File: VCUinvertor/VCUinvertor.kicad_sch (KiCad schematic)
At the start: 96 parts, among them J1 NXP12, J2 NXP11, J3 NXP15, J4 NXP14, J5 NXP10, J6 NXP13, J7 PowerSupply, J8 CAN_NXP, J9 BACKLIGHT, Q1 BSS138, Q10 BSS138, Q2 BSS138, Q3 BSS138, Q4 BSS138, Q5 BSS138, Q6 BSS138, Q7 BSS138, Q8 BSS138, Q9 BSS138, U1 TJA1448ATK, U2 REF3433T, U3 TLV76150DCY

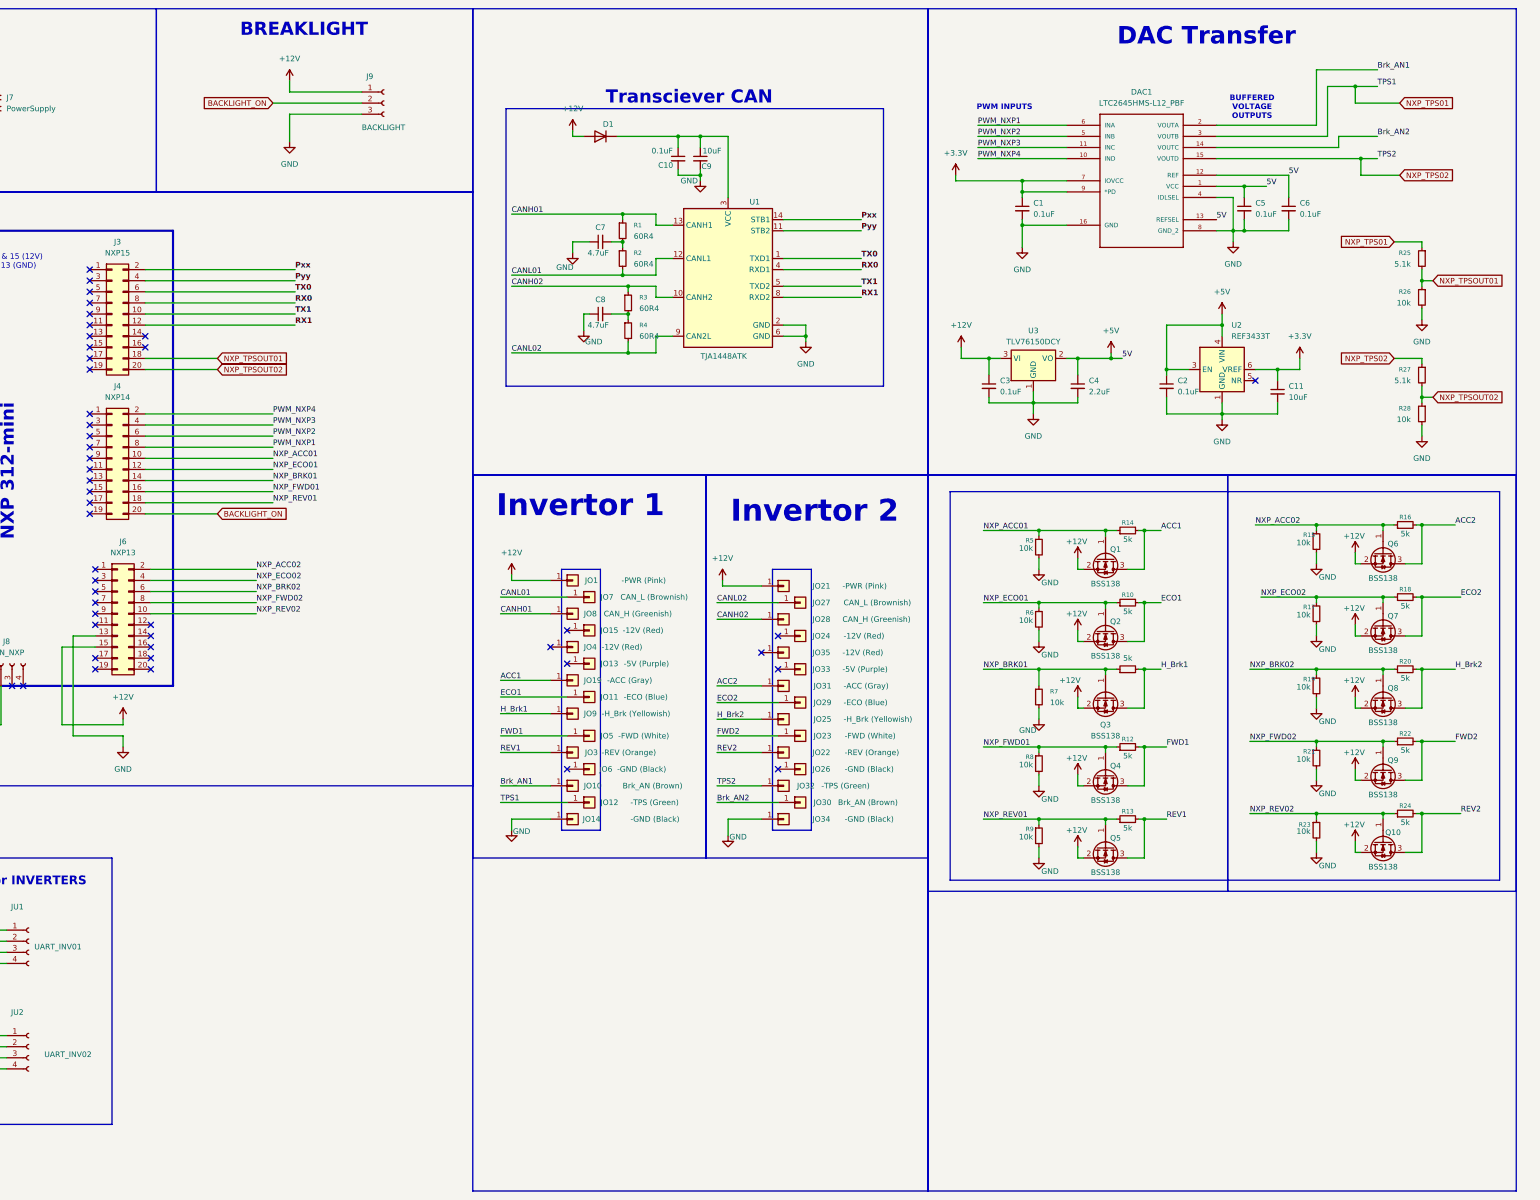
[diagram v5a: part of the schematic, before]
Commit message: New PMOS config for switching
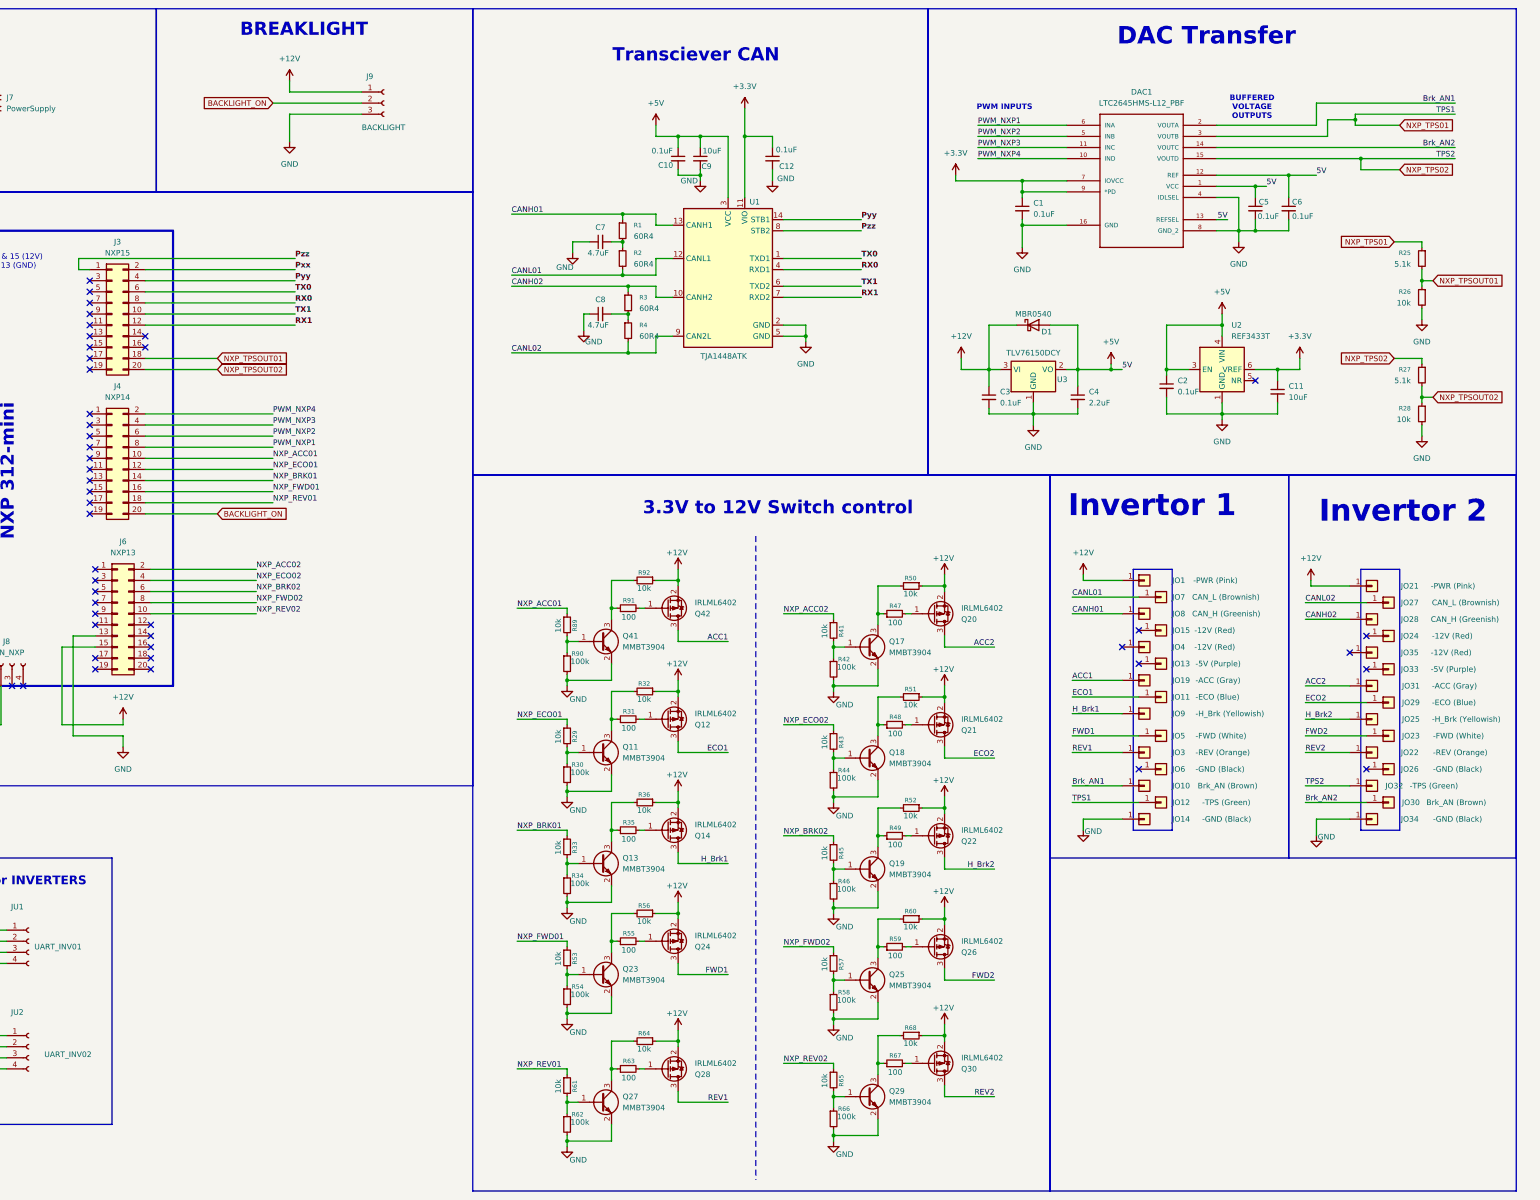
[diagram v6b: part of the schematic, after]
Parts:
- removed D1: 1N4148WT, Diode_SMD:D_SOD-523, symbol Diode:1N4148WT
- removed Q1, Q10, Q2, Q3, Q4, Q5, Q6, Q7, Q8, Q9: BSS138, Package_TO_SOT_SMD:SOT-23, symbol Transistor_FET:BSS138
- removed R10, R11, R12, R13, R14, R16, R18, R20, R22, R24: 5k, Resistor_SMD:R_0805_2012Metric, symbol Device:R_Small
- removed R15, R17, R19, R21, R23, R5, R6, R7, R8, R9: 10k, Resistor_SMD:R_0805_2012Metric, symbol Device:R_Small
- added C12: 0.1uF, Capacitor_SMD:C_0805_2012Metric_Pad1.18x1.45mm_HandSolder, symbol Device:C_Small
- added D1: MBR0540, Diode_SMD:D_SOD-123, symbol Diode:MBR0540
- added Q11, Q13, Q17, Q18, Q19, Q23, Q25, Q27, Q29, Q41: MMBT3904, Package_TO_SOT_SMD:SOT-23, symbol Transistor_BJT:MMBT3904
- added Q12, Q14, Q20, Q21, Q22, Q24, Q26, Q28, Q30, Q42: IRLML6402, Package_TO_SOT_SMD:SOT-23, symbol Transistor_FET:IRLML6402
- added R29, R32, R33, R36, R41, R43, R45, R50, R51, R52, R53, R56, R57, R60, R61, R64, R65, R68, R89, R92: 10k, Resistor_SMD:R_0805_2012Metric, symbol Device:R_Small
- added R30, R34, R42, R44, R46, R54, R58, R62, R66, R90: 100k, Resistor_SMD:R_0805_2012Metric, symbol Device:R_Small
- added R31, R35, R47, R48, R49, R55, R59, R63, R67, R91: 100, Resistor_SMD:R_0805_2012Metric, symbol Device:R_Small
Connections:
- net +12V: now also D1.1 (K), Q12.2 (S), Q14.2 (S), Q20.2 (S), Q21.2 (S), Q22.2 (S), Q24.2 (S), Q26.2 (S), Q28.2 (S), Q30.2 (S), Q42.2 (S), R32.1, R36.1, R50.1, R51.1, R52.1, R56.1, R60.1, R64.1, R68.1, R92.1
- net +3.3V: now also U1.11 (VIO), C12.1
- net +5V: now also C10.1, C9.1, U1.3 (VCC), D1.2 (A)
- net ACC1: now also Q42.3 (D)
- net ACC2: now also Q20.3 (D)
- net ECO1: now also Q12.3 (D)
- net ECO2: now also Q21.3 (D)
- net FWD1: now also Q24.3 (D)
- net FWD2: now also Q26.3 (D)
- net GND: now also U1.5 (GND), C12.2, Q11.2 (E), Q13.2 (E), Q17.2 (E), Q18.2 (E), Q19.2 (E), Q23.2 (E), Q25.2 (E), Q27.2 (E), Q29.2 (E), Q41.2 (E), R30.2, R34.2, R42.2, R44.2, R46.2, R54.2, R58.2, R62.2, R66.2, R90.2; no longer U1.6 (GND)
- net H_Brk1: now also Q14.3 (D)
- net H_Brk2: now also Q22.3 (D)
- net NXP_ACC01: now also R89.1
- net NXP_ACC02: now also R41.1
- net NXP_BRK01: now also R33.1
- net NXP_BRK02: now also R45.1
- net NXP_ECO01: now also R29.1
- net NXP_ECO02: now also R43.1
- net NXP_FWD01: now also R53.1
- net NXP_FWD02: now also R57.1
- net NXP_REV01: now also R61.1
- net NXP_REV02: now also R65.1
- net Pxx: no longer U1.14 (STB1)
- net Pyy: now also U1.14 (STB1); no longer U1.11 (STB2)
- net REV1: now also Q28.3 (D)
- net REV2: now also Q30.3 (D)
- net RX1: now also U1.7 (RXD2); no longer U1.8 (RXD2)
- net TX1: now also U1.6 (TXD2); no longer U1.5 (TXD2)
- net Pzz: now reaches J3.1 (Pin_1)
- net Pzz: now also U1.8 (STB2)
- new net: Q18.1 (B), R43.2, R44.1
- new net: Q41.1 (B), R89.2, R90.1
- new net: Q41.3 (C), R91.1, R92.2
- new net: Q11.1 (B), R29.2, R30.1
- new net: Q22.1 (G), R49.2
- new net: Q18.3 (C), R48.1, R51.2
- new net: Q21.1 (G), R48.2
- new net: Q13.1 (B), R33.2, R34.1
- new net: Q23.3 (C), R55.1, R56.2
- new net: Q42.1 (G), R91.2
- new net: Q17.3 (C), R47.1, R50.2
- new net: Q11.3 (C), R31.1, R32.2
- new net: Q25.1 (B), R57.2, R58.1
- new net: Q25.3 (C), R59.1, R60.2
- new net: Q13.3 (C), R35.1, R36.2
- new net: Q14.1 (G), R35.2
- new net: Q30.1 (G), R67.2
- new net: Q29.1 (B), R65.2, R66.1
- new net: Q17.1 (B), R41.2, R42.1
- new net: Q12.1 (G), R31.2
- new net: Q27.3 (C), R63.1, R64.2
- new net: Q26.1 (G), R59.2
- new net: Q29.3 (C), R67.1, R68.2
- new net: Q23.1 (B), R53.2, R54.1
- new net: Q28.1 (G), R63.2
- new net: Q20.1 (G), R47.2
- new net: Q27.1 (B), R61.2, R62.1
- new net: Q24.1 (G), R55.2
- new net: Q19.3 (C), R49.1, R52.2
- new net: Q19.1 (B), R45.2, R46.1
- no-connect marks 105 -> 104
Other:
- note added: "3.3V to 12V Switch control"
- moved on the sheet: C3, C4, C5, JO1, JO10, JO11, JO12, JO13, JO14, JO15, JO19, JO21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

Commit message: VCU_PinCorrection_0.1
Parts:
- renumbered J5 to NXP10, J2 to NXP11, J1 to NXP12, J6 to NXP13, J4 to NXP14, J3 to NXP15
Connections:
- net Brk_AN1: now also DAC1.14 (VOUTC); no longer DAC1.2 (VOUTA)
- net Brk_AN2: now also DAC1.2 (VOUTA); no longer DAC1.14 (VOUTC)
- net CANH01: now also R3.1, U1.10 (CANH2); no longer R1.1, U1.13 (CANH1)
- net CANH02: now also R1.1, U1.13 (CANH1); no longer R3.1, U1.10 (CANH2)
- net CANL01: now also R4.2, U1.9 (CAN2L); no longer R2.2, U1.12 (CANL1)
- net CANL02: now also R2.2, U1.12 (CANL1); no longer R4.2, U1.9 (CAN2L)
- net NXP_ACC01: no longer NXP14.10 (Pin_10)
- net NXP_ACC02: no longer NXP13.2 (Pin_2)
- net NXP_BRK01: no longer NXP14.14 (Pin_14)
- net NXP_BRK02: no longer NXP13.6 (Pin_6)
- net NXP_ECO01: no longer NXP14.12 (Pin_12)
- net NXP_ECO02: no longer NXP13.4 (Pin_4)
- net NXP_FWD01: no longer NXP14.16 (Pin_16)
- net NXP_FWD02: no longer NXP13.8 (Pin_8)
- net NXP_REV01: no longer NXP14.18 (Pin_18)
- net NXP_REV02: no longer NXP13.10 (Pin_10)
- net NXP_TPS01: now also DAC1.15 (VOUTD); no longer DAC1.3 (VOUTB)
- net NXP_TPS02: now also DAC1.3 (VOUTB); no longer DAC1.15 (VOUTD)
- net NXP_TPSOUT01: now also NXP14.1 (Pin_1); no longer NXP15.18 (Pin_18)
- net NXP_TPSOUT02: now also NXP14.3 (Pin_3); no longer NXP15.20 (Pin_20)
- net PWM_NXP1: no longer NXP14.8 (Pin_8)
- net PWM_NXP2: no longer NXP14.6 (Pin_6)
- net PWM_NXP3: no longer NXP14.4 (Pin_4)
- net PWM_NXP4: no longer NXP14.2 (Pin_2)
- net Pxx: no longer NXP15.2 (Pin_2)
- net Pyy: no longer NXP15.4 (Pin_4)
- net Pzz: no longer NXP15.1 (Pin_1)
- net RX0: now also NXP10.4 (Pin_4); no longer NXP15.8 (Pin_8)
- net RX1: now also NXP10.13 (Pin_13); no longer NXP15.12 (Pin_12)
- net TX0: now also NXP10.2 (Pin_2); no longer NXP15.6 (Pin_6)
- net TX1: now also NXP10.15 (Pin_15); no longer NXP15.10 (Pin_10)
- net BACKLIGHT_ON: no longer names the net of NXP14.20 (Pin_20)
- net BACKLIGHT_ON: no longer J9.2 (Pin_2)
- new net BREAKLIGHT: J9.2 (Pin_2)
- no-connect marks 104 -> 93
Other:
- note added: "Unassigned pins"

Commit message: Pin_Assignment_Main_Done
[15:48, 3/30/2026] Viorel VCU: ptb22 - j12 - pin 1 - LPUART1_TX - UART_INV01 pin 3
ptb23 - j12 - pin 3 - LPUART1_RX - UART_INV01 pin 2
ptd2 - j11 - pin 5 - LPUART3_TX - UART_INV02 pin 3
ptd3 - j11 - pin 7 - LPUART3_RX - UART_INV01 pin 2
[15:55, 3/30/2026] Viorel VCU: pte23 - j15 - pin 9 - EMIOS1_CH3_H - PWM_NXP1
pte24 - j15 - pin 11 - EMIOS1_CH4_H - PWM_NXP2
pte25 - j15 - pin 13 - EMIOS1_CH5_H - PWM_NXP3
pte26 - j15 - pin 15 - EMIOS1_CH6_H - PWM_NXP4
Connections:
- net PWM_NXP1: now also NXP15.9 (Pin_9)
- net PWM_NXP2: now also NXP15.11 (Pin_11)
- net PWM_NXP3: now also NXP15.13 (Pin_13)
- net PWM_NXP4: now also NXP15.15 (Pin_15)
- net Rx_UART01: now reaches NXP12.2 (Pin_2)
- net Rx_UART01: now also JU1.3 (Pin_3)
- net Tx_UART01: now reaches NXP12.3 (Pin_3)
- net Tx_UART01: now also JU1.2 (Pin_2)
- net Rx_UART02: now reaches NXP11.2 (Pin_2)
- net Rx_UART02: now also JU2.3 (Pin_3)
- net Tx_UART02: now reaches NXP11.3 (Pin_3)
- net Tx_UART02: now also JU2.2 (Pin_2)
- removed net Rx: JU1.3 (Pin_3), JU2.3 (Pin_3)
- removed net Tx: JU1.2 (Pin_2), JU2.2 (Pin_2)
- net V+ renamed V+1
- net V+1: no longer JU2.1 (Pin_1)
- net V- renamed V-1
- net V-1: no longer JU2.4 (Pin_4)
- new net V+2: JU2.1 (Pin_1)
- new net V-2: JU2.4 (Pin_4)
- no-connect marks 93 -> 85
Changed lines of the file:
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@@
 	)
 	(no_connect
-		(at 80.01 91.44)
-	)
-	(no_connect
 		(at 29.21 162.56)
 	)
@@
 	)
 	(no_connect
-		(at 80.01 83.82)
-	)
-	(no_connect
 		(at 29.21 78.74)
 	)
@@
 	)
 	(no_connect
-		(at 41.91 73.66)
+		(at 80.01 111.76)
 	)
 	(no_connect
-		(at 80.01 111.76)
+		(at 80.01 81.28)
 	)
 	(no_connect
@@
 	)
 	(no_connect
-		(at 80.01 81.28)
-	)
-	(no_connect
 		(at 80.01 114.3)
 	)
@@
 	)
 	(no_connect
-		(at 29.21 110.49)
-	)
-	(no_connect
 		(at 41.91 165.1)
 	)
@@
 	)
 	(no_connect
-		(at 80.01 88.9)
-	)
-	(no_connect
 		(at 41.91 110.49)
 	)
@@
 	)
 	(no_connect
-		(at 41.91 107.95)
-	)
-	(no_connect
 		(at 29.21 81.28)
 	)
@@
 	)
 	(no_connect
-		(at 80.01 86.36)
-	)
-	(no_connect
 		(at 41.91 123.19)
 	)
@@
 	)
 	(no_connect
-		(at 29.21 76.2)
-	)
-	(no_connect
 		(at 92.71 88.9)
 	)
@@
 	(wire
 		(pts
+			(xy 12.7 110.49) (xy 29.21 110.49)
+		)
+		(stroke
+			(width 0)
+			(type default)
+		)
+	)
+	(wire
+		(pts
 			(xy 369.57 39.37) (xy 369.57 40.64)
 		)
@@
 	(wire
 		(pts
+			(xy 44.45 105.41) (xy 44.45 107.95)
+		)
+		(stroke
+			(width 0)
+			(type default)
+		)
+	)
+	(wire
+		(pts
 			(xy 359.41 146.05) (xy 359.41 144.78)
 		)
@@
 	(wire
 		(pts
+			(xy 41.91 73.66) (xy 44.45 73.66)
+		)
+		(stroke
+			(width 0)
+			(type default)
+		)
+	)
+	(wire
+		(pts
 			(xy 250.19 193.04) (xy 250.19 194.31)
 		)
@@
 	(wire
 		(pts
+			(xy 12.7 71.12) (xy 44.45 71.12)
+		)
+		(stroke
+			(width 0)
+			(type default)
+		)
+	)
+	(wire
+		(pts
 			(xy 275.59 146.05) (xy 275.59 147.32)
 		)
@@
 	(wire
 		(pts
+			(xy 44.45 107.95) (xy 41.91 107.95)
+		)
+		(stroke
+			(width 0)
+			(type default)
+		)
+	)
+	(wire
+		(pts
 			(xy 209.55 40.64) (xy 209.55 43.18)
 		)
@@
 	(wire
 		(pts
+			(xy 12.7 76.2) (xy 29.21 76.2)
+		)
+		(stroke
+			(width 0)
+			(type default)
+		)
+	)
+	(wire
+		(pts
 			(xy 339.09 83.82) (xy 339.09 86.36)
 		)
@@
 	(wire
 		(pts
+			(xy 78.74 86.36) (xy 80.01 86.36)
+		)
+		(stroke
+			(width 0)
+			(type default)
+		)
+	)
+	(wire
+		(pts
 			(xy 250.19 210.82) (xy 252.73 210.82)
 		)
@@
 	(wire
 		(pts
+			(xy 78.74 83.82) (xy 80.01 83.82)
+		)
+		(stroke
+			(width 0)
+			(type default)
+		)
+	)
+	(wire
+		(pts
 			(xy 351.79 96.52) (xy 351.79 99.06)
 		)
@@
 	(wire
 		(pts
+			(xy 44.45 73.66) (xy 44.45 71.12)
+		)
+		(stroke
+			(width 0)
+			(type default)
+		)
+	)
+	(wire
+		(pts
 			(xy 358.14 153.67) (xy 368.3 153.67)
 		)
@@
 	(wire
 		(pts
+			(xy 12.7 105.41) (xy 44.45 105.41)
+		)
+		(stroke
+			(width 0)
+			(type default)
+		)
+	)
+	(wire
+		(pts
 			(xy 205.74 256.54) (xy 207.01 256.54)
 		)
@@
 	(wire
 		(pts
+			(xy 78.74 88.9) (xy 80.01 88.9)
+		)
+		(stroke
+			(width 0)
+			(type default)
+		)
+	)
+	(wire
+		(pts
 			(xy 337.82 45.72) (xy 392.43 45.72)
 		)
@@
 	(wire
 		(pts
+			(xy 78.74 91.44) (xy 80.01 91.44)
+		)
+		(stroke
+			(width 0)
+			(type default)
+		)
+	)
+	(wire
+		(pts
 			(xy 243.84 88.9) (xy 243.84 90.17)
 		)
@@
 		)
 	)
-	(label "V+"
+	(label "V+2"
 		(at 48.26 248.92 0)
 		(effects
@@
 		)
 	)
+	(label "Rx_UART02"
+		(at 43.18 254 0)
+		(effects
+			(font
+				(size 1.27 1.27)
+			)
+			(justify left bottom)
+		)
+	)
 	(label "RX1"
 		(at 15.24 157.48 0)
@@
 		)
 	)
+	(label "Tx_UART02"
+		(at 12.7 110.49 0)
+		(effects
+			(font
+				(size 1.27 1.27)
+			)
+			(justify left bottom)
+		)
+	)
 	(label "H_Brk2"
 		(at 358.14 176.53 0)
@@
 	)
 	(label "PWM_NXP1"
-		(at 121.92 114.3 0)
+		(at 78.74 83.82 180)
 		(effects
 			(font
 				(size 1.27 1.27)
 			)
-			(justify left bottom)
+			(justify right bottom)
 		)
 	)
@@
 	)
 	(label "PWM_NXP4"
-		(at 121.92 106.68 0)
+		(at 78.74 91.44 180)
 		(effects
 			(font
 				(size 1.27 1.27)
 			)
-			(justify left bottom)
+			(justify right bottom)
 		)
 	)
@@
 		)
 	)
+	(label "Tx_UART02"
+		(at 45.72 251.46 0)
+		(effects
+			(font
+				(size 1.27 1.27)
+			)
+			(justify left bottom)
+		)
+	)
 	(label "NXP_BRK02"
 		(at 238.76 203.2 0)
@@
 		)
 	)
-	(label "V-"
+	(label "V-1"
 		(at 40.64 232.41 0)
 		(effects
@@
 		)
 	)
-	(label "Tx"
+	(label "Tx_UART01"
 		(at 45.72 227.33 0)
 		(effects
@@
 		)
 	)
+	(label "Tx_UART01"
+		(at 12.7 76.2 0)
+		(effects
+			(font
+				(size 1.27 1.27)
+			)
+			(justify left bottom)
+		)
+	)
 	(label "H_Brk1"
 		(at 226.06 209.55 180)
@@
 		)
 	)
-	(label "Rx"
-		(at 43.18 254 0)
+	(label "Rx_UART02"
+		(at 12.7 105.41 0)
 		(effects
 			(font
@@
 	)
 	(label "PWM_NXP3"
-		(at 121.92 109.22 0)
+		(at 78.74 88.9 180)
 		(effects
 			(font
 				(size 1.27 1.27)
 			)
-			(justify left bottom)
+			(justify right bottom)
 		)
 	)
@@
 		)
 	)
-	(label "Rx"
+	(label "Rx_UART01"
 		(at 43.18 229.87 0)
 		(effects
@@
 	)
 	(label "PWM_NXP2"
-		(at 121.92 111.76 0)
+		(at 78.74 86.36 180)
 		(effects
 			(font
 				(size 1.27 1.27)
 			)
-			(justify left bottom)
+			(justify right bottom)
 		)
 	)
@@
 		)
 	)
-	(label "Tx"
-		(at 45.72 251.46 0)
-		(effects
-			(font
-				(size 1.27 1.27)
-			)
-			(justify left bottom)
-		)
-	)
 	(label "CAN_H"
 		(at 31.75 184.15 0)
@@
 		)
 	)
-	(label "V-"
+	(label "V-2"
 		(at 40.64 256.54 0)
 		(effects
@@
 		)
 	)
-	(label "V+"
+	(label "V+1"
 		(at 48.26 224.79 0)
 		(effects
@@
 		(effects
 			(font
+				(size 1.27 1.27)
+			)
+			(justify left bottom)
+		)
+	)
+	(label "Rx_UART01"
+		(at 12.7 71.12 0)
+		(effects
+			(font
